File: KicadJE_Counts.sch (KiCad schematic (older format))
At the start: 18 parts, among them J101 In7, J102 In6, J103 In3, J104 Out10, J105 Out11, J106 Out9, J107 Out6

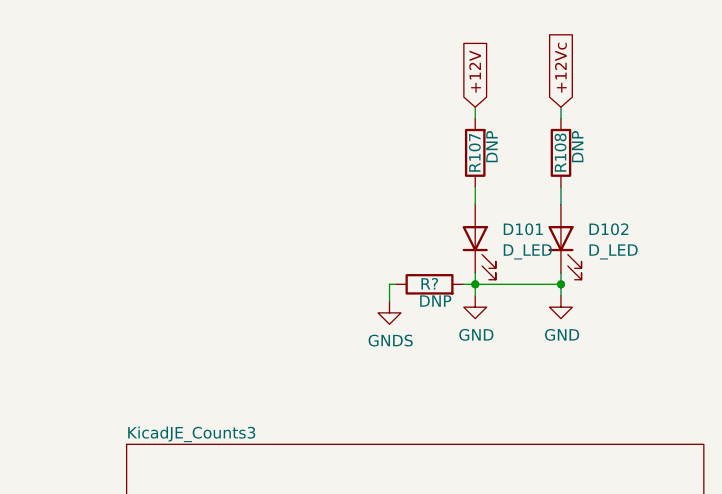
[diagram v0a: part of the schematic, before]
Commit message: Update KicadJE_Counts.sch
conn for led
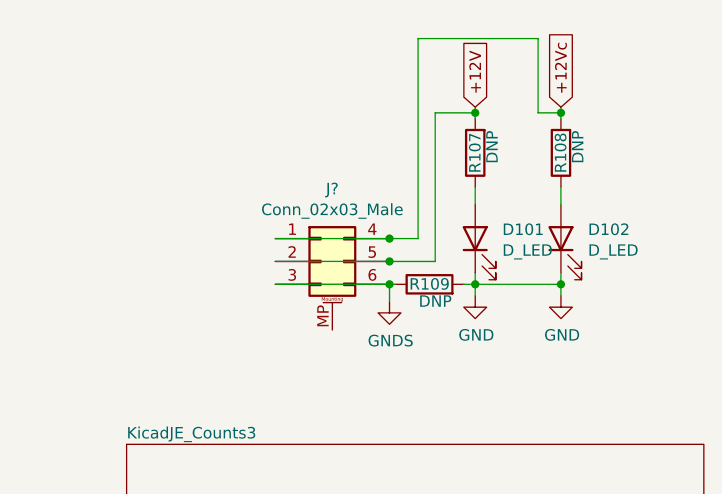
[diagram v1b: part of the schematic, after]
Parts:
- added J?: Conn_02x03_Male, Connector_PinHeader_2.54mm:PinHeader_2x03_P2.54mm_Vertical_SMD, symbol Connector_Generic_MountingPin:Conn_02x03_Top_Bottom_MountingPin
- gave numbers to parts that had none: 1
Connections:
- net +12V: now also J?.2 (Pin_2), J?.5 (Pin_5)
- net +12Vc: now also J?.1 (Pin_1), J?.4 (Pin_4)
- net GNDS: now also J?.3 (Pin_3), J?.6 (Pin_6)
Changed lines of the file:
@@
 	10550 1500 10550 1425
 Wire Wire Line
-	10550 1125 10550 1075
+	10550 1125 10550 1100
 $Comp
 L Device:LED D?
@@
 	10175 1500 10175 1425
 Wire Wire Line
-	10175 1125 10175 1075
+	10175 1125 10175 1100
 Text GLabel 10550 1075 1    50   Input ~ 0
 +12Vc
 $Comp
-L power:GNDS #PWR?
+L power:GNDS #PWR0104
 U 1 1 5ECE79CC
 P 9800 1925
-AR Path="/5ECE79CC" Ref="#PWR?"  Part="1"
+AR Path="/5ECE79CC" Ref="#PWR0104"  Part="1"
 AR Path="/5D60ED9A/5ECE79CC" Ref="#PWR?"  Part="1"
 AR Path="/5C781441/5ECE79CC" Ref="#PWR?"  Part="1"
-F 0 "#PWR?" H 9800 1675 50  0001 C CNN
+F 0 "#PWR0104" H 9800 1675 50  0001 C CNN
 F 1 "GNDS" H 9805 1752 50  0000 C CNN
 F 2 "" H 9800 1925 50  0001 C CNN
@@
 AR Path="/5D4DB615/5ECE8C8F" Ref="R?"  Part="1"
 AR Path="/5D60ED9A/5ECE8C8F" Ref="R?"  Part="1"
-AR Path="/5ECE8C8F" Ref="R?"  Part="1"
-F 0 "R?" V 9975 1850 50  0000 C CNN
+AR Path="/5ECE8C8F" Ref="R109"  Part="1"
+F 0 "R109" V 9975 1850 50  0000 C CNN
 F 1 "DNP" V 9900 1825 50  0000 C CNN
 F 2 "AJ:R_0805_AJ" V 9905 1850 50  0001 C CNN
@@
 Wire Wire Line
 	10175 1850 10550 1850
+$Comp
+L Connector_Generic_MountingPin:Conn_02x03_Top_Bottom_MountingPin J?
+U 1 1 5ECEE662
+P 9500 1750
+F 0 "J?" H 9550 2067 50  0000 C CNN
+F 1 "Conn_02x03_Male" H 9550 1976 50  0000 C CNN
+F 2 "Connector_PinHeader_2.54mm:PinHeader_2x03_P2.54mm_Vertical_SMD" H 9500 1750 50  0001 C CNN
+F 3 "~" H 9500 1750 50  0001 C CNN
+	1    9500 1750
+	1    0    0    -1
+$EndComp
+Connection ~ 9800 1850
+Wire Wire Line
+	9800 1750 10000 1750
+Wire Wire Line
+	10000 1750 10000 1100
+Wire Wire Line
+	10000 1100 10175 1100
+Connection ~ 10175 1100
+Wire Wire Line
+	10175 1100 10175 1075
+Wire Wire Line
+	9800 1650 9925 1650
+Wire Wire Line
+	9925 1650 9925 775
+Wire Wire Line
+	9925 775  10450 775
+Wire Wire Line
+	10450 775  10450 1100
+Wire Wire Line
+	10450 1100 10550 1100
+Connection ~ 10550 1100
+Wire Wire Line
+	10550 1100 10550 1075
+Wire Wire Line
+	9800 1850 9300 1850
+Wire Wire Line
+	9300 1750 9800 1750
+Connection ~ 9800 1750
+Wire Wire Line
+	9300 1650 9800 1650
+Connection ~ 9800 1650
 $EndSCHEMATC
